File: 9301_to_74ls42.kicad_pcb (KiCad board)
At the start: 2 copper layers, 13.8 x 21.2 mm, 2 parts, among them J1 Conn_02x08_Counter_Clockwise, U1 74LS42

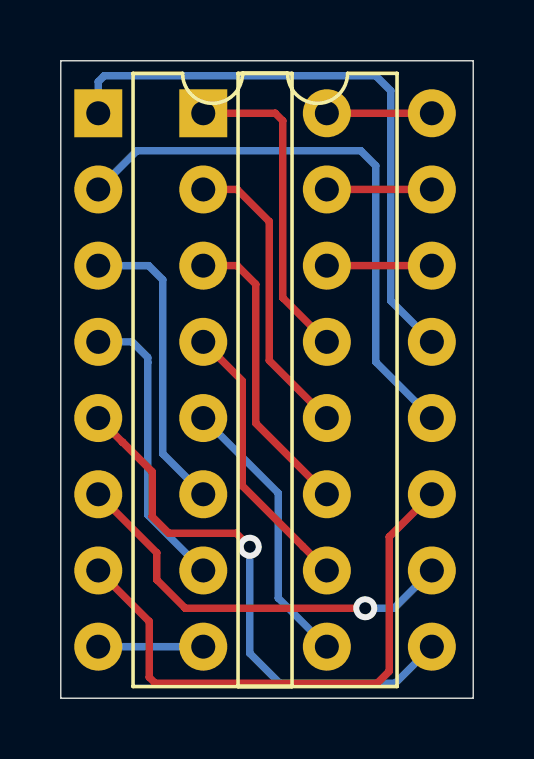
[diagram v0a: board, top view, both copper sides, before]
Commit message: Cleaned up the silkscreen
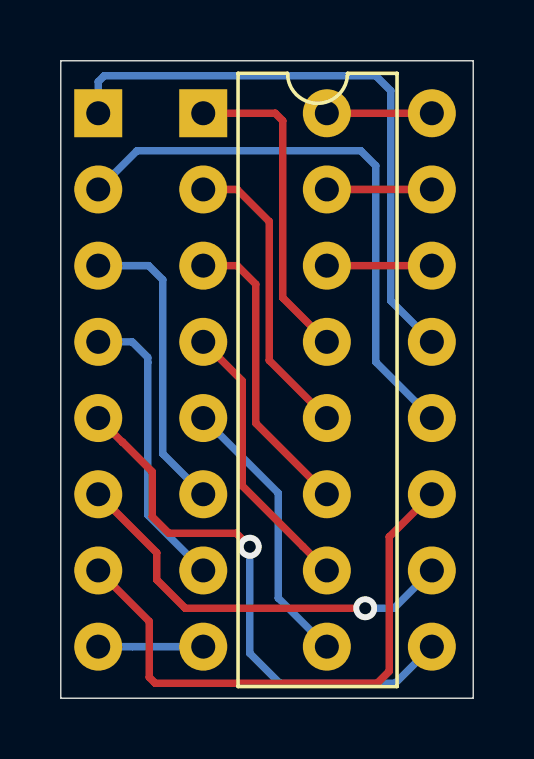
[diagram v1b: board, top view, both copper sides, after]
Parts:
- J1: footprint Housings_DIP:DIP-16_W7.62mm -> Custom Footprints:DIP-16_W7.62mm_NoSilk
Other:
- board text added: "7442"
- board text added: "Pin Headers"
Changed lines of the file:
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@@
   (general
     (thickness 1.6)
-    (drawings 4)
+    (drawings 12)
     (tracks 73)
     (zones 0)
@@
     (solder_mask_min_width 0.25)
     (aux_axis_origin 0 0)
-    (visible_elements FFFFFF7F)
+    (visible_elements 7FFFFFFF)
     (pcbplotparams
       (layerselection 0x010fc_ffffffff)
@@
     (add_net GND)
   )
-  (module Housings_DIP:DIP-16_W7.62mm (layer F.Cu)
+  (module "Custom Footprints:DIP-16_W7.62mm_NoSilk" (layer F.Cu)
     (at 136.25 47.5)
     (descr "16-lead though-hole mounted DIP package, row spacing 7.62 mm (300 mils)")
@@
       (effects (font (size 1 1) (thickness 0.15)))
     )
+    (fp_line (start 1.635 -1.27) (end 6.985 -1.27) (layer F.Fab) (width 0.1))
+    (fp_line (start 6.985 -1.27) (end 6.985 19.05) (layer F.Fab) (width 0.1))
+    (fp_line (start 6.985 19.05) (end 0.635 19.05) (layer F.Fab) (width 0.1))
+    (fp_line (start 0.635 19.05) (end 0.635 -0.27) (layer F.Fab) (width 0.1))
+    (fp_line (start 0.635 -0.27) (end 1.635 -1.27) (layer F.Fab) (width 0.1))
+    (fp_line (start -1.1 -1.55) (end -1.1 19.3) (layer F.CrtYd) (width 0.05))
+    (fp_line (start -1.1 19.3) (end 8.7 19.3) (layer F.CrtYd) (width 0.05))
+    (fp_line (start 8.7 19.3) (end 8.7 -1.55) (layer F.CrtYd) (width 0.05))
+    (fp_line (start 8.7 -1.55) (end -1.1 -1.55) (layer F.CrtYd) (width 0.05))
     (fp_text user %R (at 3.81 8.89) (layer F.Fab)
       (effects (font (size 1 1) (thickness 0.15)))
     )
-    (fp_line (start 8.7 -1.55) (end -1.1 -1.55) (layer F.CrtYd) (width 0.05))
-    (fp_line (start 8.7 19.3) (end 8.7 -1.55) (layer F.CrtYd) (width 0.05))
-    (fp_line (start -1.1 19.3) (end 8.7 19.3) (layer F.CrtYd) (width 0.05))
-    (fp_line (start -1.1 -1.55) (end -1.1 19.3) (layer F.CrtYd) (width 0.05))
-    (fp_line (start 6.46 -1.33) (end 4.81 -1.33) (layer F.SilkS) (width 0.12))
-    (fp_line (start 6.46 19.11) (end 6.46 -1.33) (layer F.SilkS) (width 0.12))
-    (fp_line (start 1.16 19.11) (end 6.46 19.11) (layer F.SilkS) (width 0.12))
-    (fp_line (start 1.16 -1.33) (end 1.16 19.11) (layer F.SilkS) (width 0.12))
-    (fp_line (start 2.81 -1.33) (end 1.16 -1.33) (layer F.SilkS) (width 0.12))
-    (fp_line (start 0.635 -0.27) (end 1.635 -1.27) (layer F.Fab) (width 0.1))
-    (fp_line (start 0.635 19.05) (end 0.635 -0.27) (layer F.Fab) (width 0.1))
-    (fp_line (start 6.985 19.05) (end 0.635 19.05) (layer F.Fab) (width 0.1))
-    (fp_line (start 6.985 -1.27) (end 6.985 19.05) (layer F.Fab) (width 0.1))
-    (fp_line (start 1.635 -1.27) (end 6.985 -1.27) (layer F.Fab) (width 0.1))
-    (fp_arc (start 3.81 -1.33) (end 2.81 -1.33) (angle -180) (layer F.SilkS) (width 0.12))
+    (pad 1 thru_hole rect (at 0 0) (size 1.6 1.6) (drill 0.8) (layers *.Cu *.Mask)
+      (net 16 A2))
+    (pad 9 thru_hole oval (at 7.62 17.78) (size 1.6 1.6) (drill 0.8) (layers *.Cu *.Mask)
+      (net 15 4))
+    (pad 2 thru_hole oval (at 0 2.54) (size 1.6 1.6) (drill 0.8) (layers *.Cu *.Mask)
+      (net 14 A3))
+    (pad 10 thru_hole oval (at 7.62 15.24) (size 1.6 1.6) (drill 0.8) (layers *.Cu *.Mask)
+      (net 13 3))
+    (pad 3 thru_hole oval (at 0 5.08) (size 1.6 1.6) (drill 0.8) (layers *.Cu *.Mask)
+      (net 12 5))
+    (pad 11 thru_hole oval (at 7.62 12.7) (size 1.6 1.6) (drill 0.8) (layers *.Cu *.Mask)
+      (net 11 2))
+    (pad 4 thru_hole oval (at 0 7.62) (size 1.6 1.6) (drill 0.8) (layers *.Cu *.Mask)
+      (net 10 6))
+    (pad 12 thru_hole oval (at 7.62 10.16) (size 1.6 1.6) (drill 0.8) (layers *.Cu *.Mask)
+      (net 9 1))
+    (pad 5 thru_hole oval (at 0 10.16) (size 1.6 1.6) (drill 0.8) (layers *.Cu *.Mask)
+      (net 8 7))
+    (pad 13 thru_hole oval (at 7.62 7.62) (size 1.6 1.6) (drill 0.8) (layers *.Cu *.Mask)
+      (net 7 0))
+    (pad 6 thru_hole oval (at 0 12.7) (size 1.6 1.6) (drill 0.8) (layers *.Cu *.Mask)
+      (net 6 8))
+    (pad 14 thru_hole oval (at 7.62 5.08) (size 1.6 1.6) (drill 0.8) (layers *.Cu *.Mask)
+      (net 5 A1))
+    (pad 7 thru_hole oval (at 0 15.24) (size 1.6 1.6) (drill 0.8) (layers *.Cu *.Mask)
+      (net 4 9))
+    (pad 15 thru_hole oval (at 7.62 2.54) (size 1.6 1.6) (drill 0.8) (layers *.Cu *.Mask)
+      (net 3 A0))
+    (pad 8 thru_hole oval (at 0 17.78) (size 1.6 1.6) (drill 0.8) (layers *.Cu *.Mask)
+      (net 2 GND))
     (pad 16 thru_hole oval (at 7.62 0) (size 1.6 1.6) (drill 0.8) (layers *.Cu *.Mask)
       (net 1 +5V))
-    (pad 8 thru_hole oval (at 0 17.78) (size 1.6 1.6) (drill 0.8) (layers *.Cu *.Mask)
-      (net 2 GND))
-    (pad 15 thru_hole oval (at 7.62 2.54) (size 1.6 1.6) (drill 0.8) (layers *.Cu *.Mask)
-      (net 3 A0))
-    (pad 7 thru_hole oval (at 0 15.24) (size 1.6 1.6) (drill 0.8) (layers *.Cu *.Mask)
-      (net 4 9))
-    (pad 14 thru_hole oval (at 7.62 5.08) (size 1.6 1.6) (drill 0.8) (layers *.Cu *.Mask)
-      (net 5 A1))
-    (pad 6 thru_hole oval (at 0 12.7) (size 1.6 1.6) (drill 0.8) (layers *.Cu *.Mask)
-      (net 6 8))
-    (pad 13 thru_hole oval (at 7.62 7.62) (size 1.6 1.6) (drill 0.8) (layers *.Cu *.Mask)
-      (net 7 0))
-    (pad 5 thru_hole oval (at 0 10.16) (size 1.6 1.6) (drill 0.8) (layers *.Cu *.Mask)
-      (net 8 7))
-    (pad 12 thru_hole oval (at 7.62 10.16) (size 1.6 1.6) (drill 0.8) (layers *.Cu *.Mask)
-      (net 9 1))
-    (pad 4 thru_hole oval (at 0 7.62) (size 1.6 1.6) (drill 0.8) (layers *.Cu *.Mask)
-      (net 10 6))
-    (pad 11 thru_hole oval (at 7.62 12.7) (size 1.6 1.6) (drill 0.8) (layers *.Cu *.Mask)
-      (net 11 2))
-    (pad 3 thru_hole oval (at 0 5.08) (size 1.6 1.6) (drill 0.8) (layers *.Cu *.Mask)
-      (net 12 5))
-    (pad 10 thru_hole oval (at 7.62 15.24) (size 1.6 1.6) (drill 0.8) (layers *.Cu *.Mask)
-      (net 13 3))
-    (pad 2 thru_hole oval (at 0 2.54) (size 1.6 1.6) (drill 0.8) (layers *.Cu *.Mask)
-      (net 14 A3))
-    (pad 9 thru_hole oval (at 7.62 17.78) (size 1.6 1.6) (drill 0.8) (layers *.Cu *.Mask)
-      (net 15 4))
-    (pad 1 thru_hole rect (at 0 0) (size 1.6 1.6) (drill 0.8) (layers *.Cu *.Mask)
-      (net 16 A2))
     (model ${KISYS3DMOD}/Housings_DIP.3dshapes/DIP-16_W7.62mm.wrl
       (at (xyz 0 0 0))
@@
     )
   )
+  (gr_text "Pin Headers" (at 141.7 62.325 270) (layer B.SilkS)
+    (effects (font (size 1 1) (thickness 0.15)) (justify mirror))
+  )
+  (gr_text 7442 (at 141.9 47.875 270) (layer B.SilkS)
+    (effects (font (size 1 1) (thickness 0.15)) (justify mirror))
+  )
+  (gr_line (start 147.375 45.875) (end 147.375 46.425) (layer B.SilkS) (width 0.12))
+  (gr_line (start 139.775 45.875) (end 147.375 45.875) (layer B.SilkS) (width 0.12))
+  (gr_line (start 139.775 46.45) (end 139.775 45.875) (layer B.SilkS) (width 0.12))
+  (gr_line (start 143.9 66.875) (end 143.9 66.35) (layer B.SilkS) (width 0.12))
+  (gr_line (start 136.275 66.875) (end 143.9 66.875) (layer B.SilkS) (width 0.12))
+  (gr_line (start 136.275 66.325) (end 136.275 66.875) (layer B.SilkS) (width 0.12))
   (gr_line (start 135 45.75) (end 135 67) (layer Edge.Cuts) (width 0.05))
   (gr_line (start 148.75 45.75) (end 135 45.75) (layer Edge.Cuts) (width 0.05))
